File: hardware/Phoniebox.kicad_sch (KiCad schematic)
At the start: 11 parts, among them J1 GPIO, J2 Screw_Terminal_01x08, J3 Screw_Terminal_01x08, J4 Screw_Terminal_01x08, J5 Conn_01x04_Male, J6 Conn_01x08_Male, J7 USB_C_Receptacle_USB2.0, U4 CAT24C32

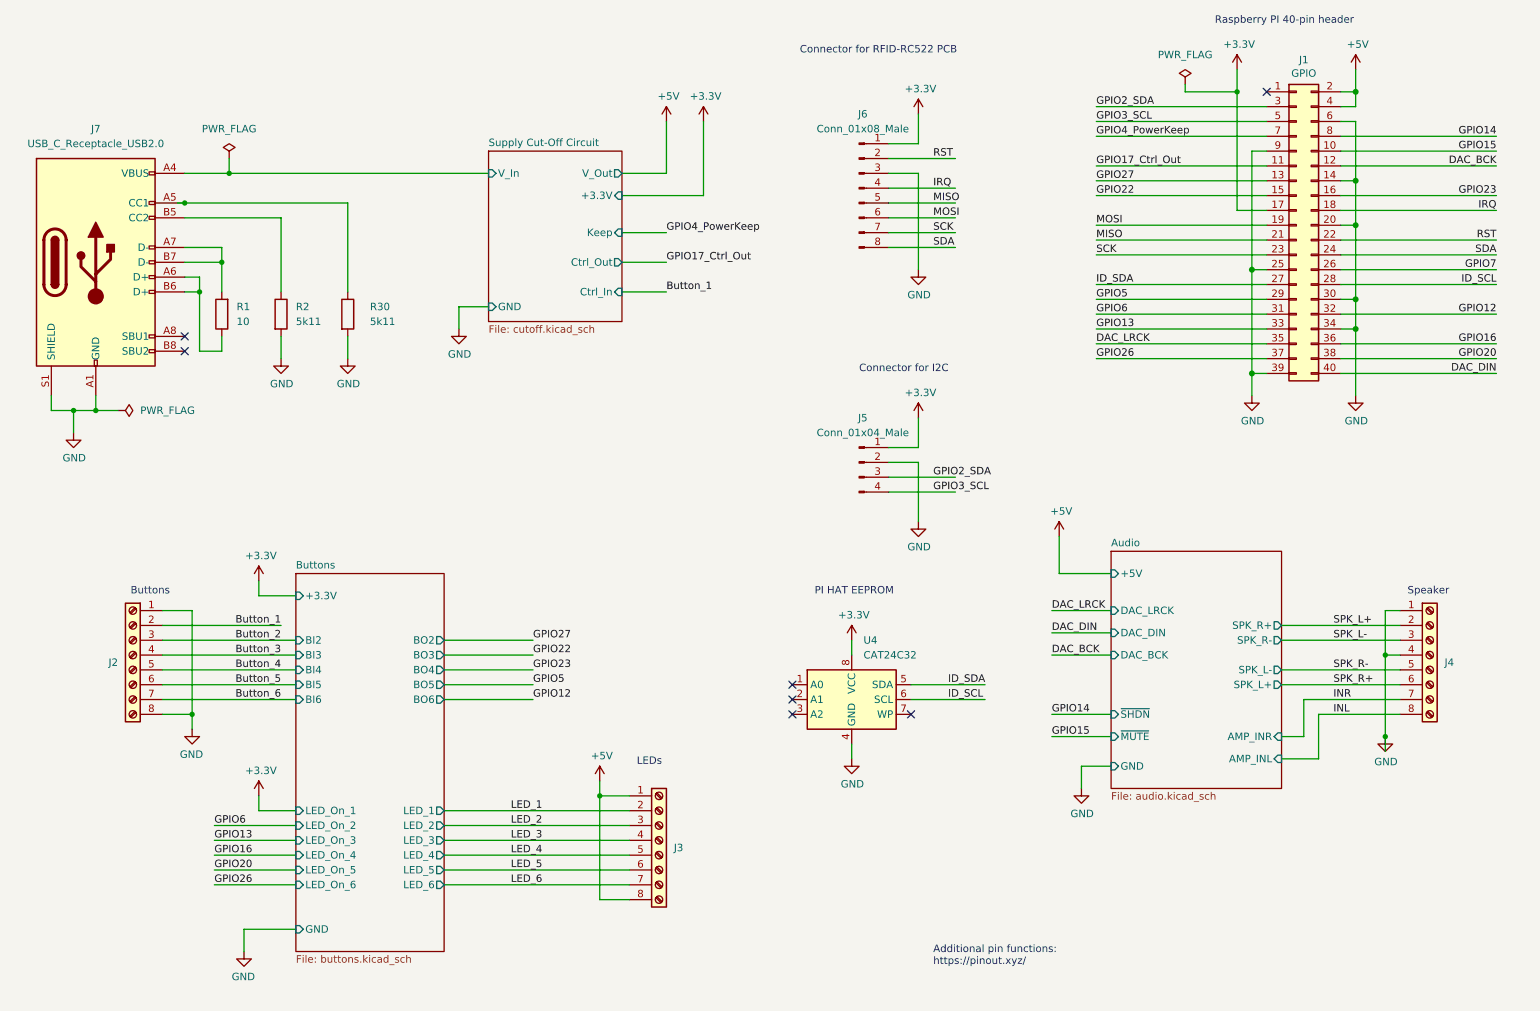
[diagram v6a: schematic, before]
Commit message: Replaced both single row connectors for RC522,I2C by one two row connector. Speaker left and right were mixed in top level schematic -> fixed net names and silkscreen text.
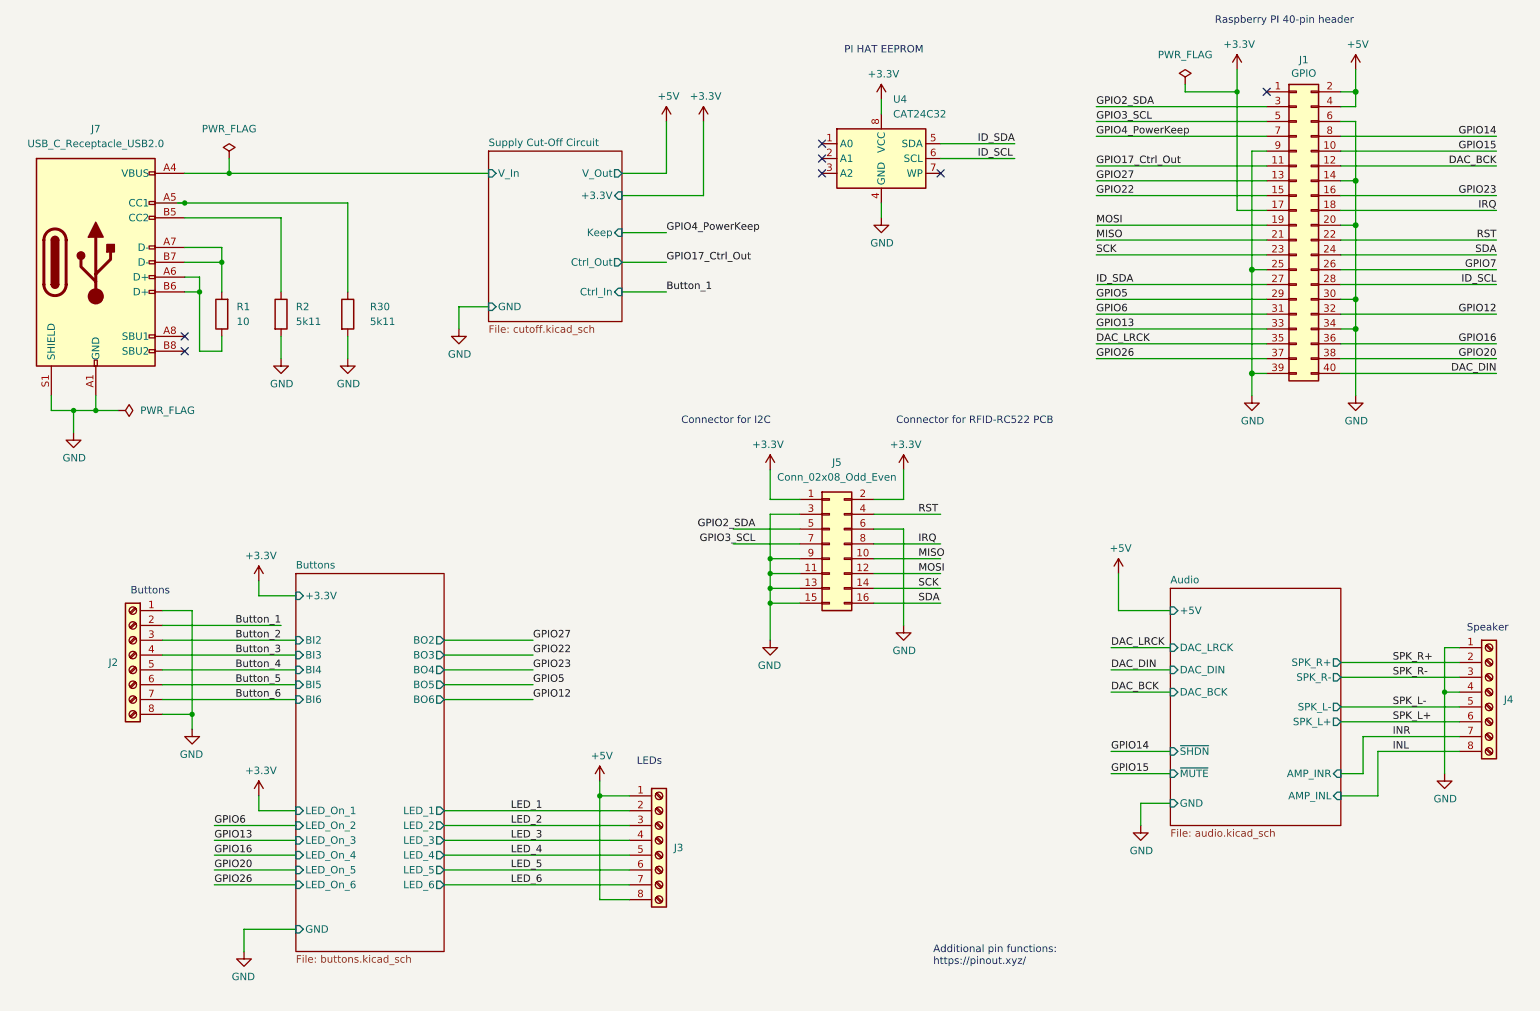
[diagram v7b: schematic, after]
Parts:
- removed J5: Conn_01x04_Male, Connector_PinHeader_2.54mm:PinHeader_1x04_P2.54mm_Vertical_SMD_Pin1Left, symbol Connector:Conn_01x04_Male
- removed J6: Conn_01x08_Male, Connector_PinHeader_2.54mm:PinHeader_1x08_P2.54mm_Vertical_SMD_Pin1Left, symbol Connector:Conn_01x08_Male
- added J5: Conn_02x08_Odd_Even, Connector_PinHeader_2.54mm:PinHeader_2x08_P2.54mm_Vertical_SMD, symbol Connector_Generic:Conn_02x08_Odd_Even
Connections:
- net +3.3V: now also J5.1 (Pin_1), J5.2 (Pin_2)
- net GND: now also J5.11 (Pin_11), J5.13 (Pin_13), J5.15 (Pin_15), J5.3 (Pin_3), J5.6 (Pin_6), J5.9 (Pin_9)
- net GPIO2_SDA: now also J5.5 (Pin_5)
- net GPIO3_SCL: now also J5.7 (Pin_7)
- net IRQ: now also J5.8 (Pin_8)
- net MISO: now also J5.10 (Pin_10)
- net MOSI: now also J5.12 (Pin_12)
- net RST: now also J5.4 (Pin_4)
- net SCK: now also J5.14 (Pin_14)
- net SDA: now also J5.16 (Pin_16)
- net SPK_L+: now also J4.6 (Pin_6); no longer J4.2 (Pin_2)
- net SPK_L-: now also J4.5 (Pin_5); no longer J4.3 (Pin_3)
- net SPK_R+: now also J4.2 (Pin_2); no longer J4.6 (Pin_6)
- net SPK_R-: now also J4.3 (Pin_3); no longer J4.5 (Pin_5)
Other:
- moved on the sheet: J4, U4
